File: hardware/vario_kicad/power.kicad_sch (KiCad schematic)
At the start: 26 parts, among them Q1 NMOS, Q2 PMOS, U4 USB C connector

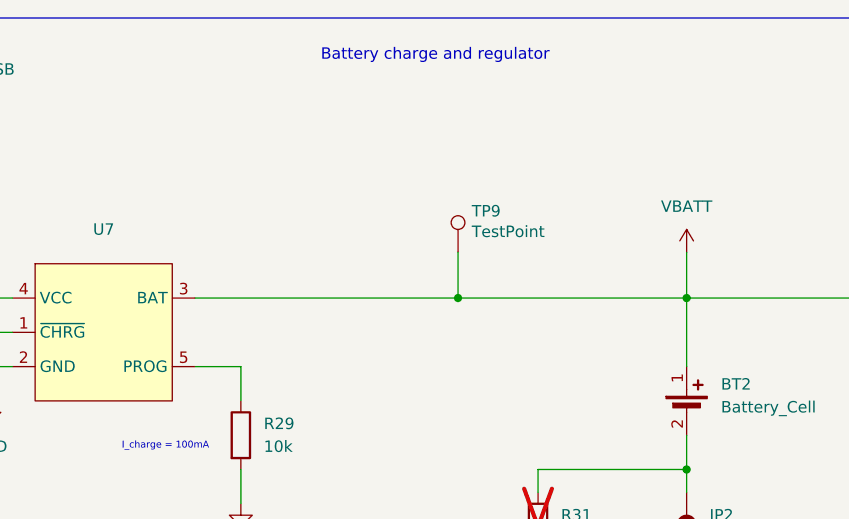
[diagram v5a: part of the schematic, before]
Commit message: add solder bridge to disconnect battery from charger
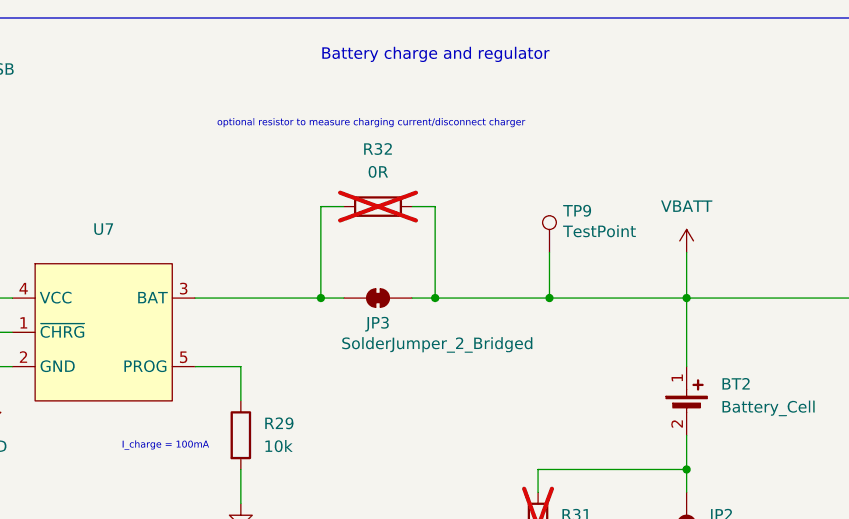
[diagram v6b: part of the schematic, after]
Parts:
- added JP3: SolderJumper_2_Bridged, Jumper:SolderJumper-2_P1.3mm_Open_TrianglePad1.0x1.5mm, symbol Jumper:SolderJumper_2_Bridged
- added R32: 0R, symbol Device:R
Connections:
- net VBATT: now also JP3.2 (B), R32.2; no longer U7.3 (BAT)
- new net: JP3.1 (A), R32.1, U7.3 (BAT)
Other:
- note added: "optional resistor to measure charging current/disconnect charger"
- moved on the sheet: TP9
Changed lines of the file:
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@@
 	)
 	(junction
+		(at 138.43 46.99)
+		(diameter 0)
+		(color 0 0 0 0)
+	)
+	(junction
 		(at 166.37 78.74)
 		(diameter 0)
@@
 	)
 	(junction
+		(at 125.73 46.99)
+		(diameter 0)
+		(color 0 0 0 0)
+	)
+	(junction
 		(at 41.91 149.86)
 		(diameter 0)
@@
 	)
 	(junction
+		(at 151.13 46.99)
+		(diameter 0)
+		(color 0 0 0 0)
+	)
+	(junction
 		(at 76.2 29.21)
 		(diameter 0)
@@
 	)
 	(junction
-		(at 140.97 46.99)
-		(diameter 0)
-		(color 0 0 0 0)
-	)
-	(junction
 		(at 214.63 59.69)
 		(diameter 0)
@@
 	(wire
 		(pts
+			(xy 128.27 46.99) (xy 125.73 46.99)
+		)
+		(stroke
+			(width 0)
+			(type default)
+		)
+	)
+	(wire
+		(pts
 			(xy 153.67 110.49) (xy 160.02 110.49)
 		)
@@
 	(wire
 		(pts
+			(xy 128.27 36.83) (xy 125.73 36.83)
+		)
+		(stroke
+			(width 0)
+			(type default)
+		)
+	)
+	(wire
+		(pts
 			(xy 30.48 149.86) (xy 41.91 149.86)
 		)
@@
 	(wire
 		(pts
+			(xy 125.73 36.83) (xy 125.73 46.99)
+		)
+		(stroke
+			(width 0)
+			(type default)
+		)
+	)
+	(wire
+		(pts
 			(xy 214.63 59.69) (xy 214.63 62.23)
 		)
@@
 	(wire
 		(pts
-			(xy 140.97 41.91) (xy 140.97 46.99)
+			(xy 151.13 41.91) (xy 151.13 46.99)
 		)
 		(stroke
@@
 	(wire
 		(pts
-			(xy 140.97 46.99) (xy 166.37 46.99)
+			(xy 151.13 46.99) (xy 166.37 46.99)
 		)
 		(stroke
@@
 	(wire
 		(pts
-			(xy 111.76 46.99) (xy 140.97 46.99)
-		)
-		(stroke
-			(width 0)
-			(type default)
-		)
-	)
-	(wire
-		(pts
 			(xy 44.45 109.22) (xy 50.8 109.22)
 		)
@@
 	(wire
 		(pts
+			(xy 138.43 46.99) (xy 135.89 46.99)
+		)
+		(stroke
+			(width 0)
+			(type default)
+		)
+	)
+	(wire
+		(pts
 			(xy 30.48 118.11) (xy 43.18 118.11)
 		)
@@
 	(wire
 		(pts
+			(xy 138.43 46.99) (xy 151.13 46.99)
+		)
+		(stroke
+			(width 0)
+			(type default)
+		)
+	)
+	(wire
+		(pts
+			(xy 138.43 36.83) (xy 135.89 36.83)
+		)
+		(stroke
+			(width 0)
+			(type default)
+		)
+	)
+	(wire
+		(pts
 			(xy 142.24 133.35) (xy 160.02 133.35)
 		)
@@
 	(wire
 		(pts
+			(xy 111.76 46.99) (xy 125.73 46.99)
+		)
+		(stroke
+			(width 0)
+			(type default)
+		)
+	)
+	(wire
+		(pts
 			(xy 166.37 46.99) (xy 166.37 54.61)
 		)
@@
 	(wire
 		(pts
+			(xy 138.43 46.99) (xy 138.43 36.83)
+		)
+		(stroke
+			(width 0)
+			(type default)
+		)
+	)
+	(wire
+		(pts
 			(xy 166.37 76.2) (xy 166.37 78.74)
 		)
@@
 		)
 	)
+	(text "optional resistor to measure charging current/disconnect charger"
+		(exclude_from_sim no)
+		(at 131.318 27.686 0)
+		(effects
+			(font
+				(size 0.762 0.762)
+			)
+		)
+	)
 	(text "Max V_BATT voltage 4.3V\nmax adc voltage 2.95V"
 		(exclude_from_sim no)
@@
 	)
 	(symbol
+		(lib_id "Jumper:SolderJumper_2_Bridged")
+		(at 132.08 46.99 0)
+		(unit 1)
+		(exclude_from_sim yes)
+		(in_bom no)
+		(on_board yes)
+		(dnp no)
+		(property "Reference" "JP3"
+			(at 132.08 49.784 0)
+			(effects
+				(font
+					(size 1.27 1.27)
+				)
+			)
+		)
+		(property "Value" "SolderJumper_2_Bridged"
+			(at 138.684 52.07 0)
+			(effects
+				(font
+					(size 1.27 1.27)
+				)
+			)
+		)
+		(property "Footprint" "Jumper:SolderJumper-2_P1.3mm_Open_TrianglePad1.0x1.5mm"
+			(at 132.08 46.99 0)
+			(effects
+				(font
+					(size 1.27 1.27)
+				)
+				(hide yes)
+			)
+		)
+		(property "Datasheet" "~"
+			(at 132.08 46.99 0)
+			(effects
+				(font
+					(size 1.27 1.27)
+				)
+				(hide yes)
+			)
+		)
+		(property "Description" "Solder Jumper, 2-pole, closed/bridged"
+			(at 132.08 46.99 0)
+			(effects
+				(font
+					(size 1.27 1.27)
+				)
+				(hide yes)
+			)
+		)
+		(pin "1"
+		)
+		(pin "2"
+		)
+		(instances
+			(project "vario_kicad"
+				(path "/50389aff-b244-451e-8e3a-c5addd2215e1/9ff7b2dd-70fe-4259-884c-1f1f10c7ad3d"
+					(reference "JP3")
+					(unit 1)
+				)
+			)
+		)
+	)
+	(symbol
 		(lib_id "Device:C")
 		(at 237.49 53.34 0)
@@
 	)
 	(symbol
+		(lib_id "Device:R")
+		(at 132.08 36.83 90)
+		(unit 1)
+		(exclude_from_sim no)
+		(in_bom yes)
+		(on_board yes)
+		(dnp yes)
+		(fields_autoplaced yes)
+		(property "Reference" "R32"
+			(at 132.08 30.48 90)
+			(effects
+				(font
+					(size 1.27 1.27)
+				)
+			)
+		)
+		(property "Value" "0R"
+			(at 132.08 33.02 90)
+			(effects
+				(font
+					(size 1.27 1.27)
+				)
+			)
+		)
+		(property "Footprint" ""
+			(at 132.08 38.608 90)
+			(effects
+				(font
+					(size 1.27 1.27)
+				)
+				(hide yes)
+			)
+		)
+		(property "Datasheet" "~"
+			(at 132.08 36.83 0)
+			(effects
+				(font
+					(size 1.27 1.27)
+				)
+				(hide yes)
+			)
+		)
+		(property "Description" "Resistor"
+			(at 132.08 36.83 0)
+			(effects
+				(font
+					(size 1.27 1.27)
+				)
+				(hide yes)
+			)
+		)
+		(pin "2"
+		)
+		(pin "1"
+		)
+		(instances
+			(project "vario_kicad"
+				(path "/50389aff-b244-451e-8e3a-c5addd2215e1/9ff7b2dd-70fe-4259-884c-1f1f10c7ad3d"
+					(reference "R32")
+					(unit 1)
+				)
+			)
+		)
+	)
+	(symbol
 		(lib_id "power:GND")
 		(at 63.5 40.64 0)
@@
 	(symbol
 		(lib_id "Connector:TestPoint")
-		(at 140.97 41.91 0)
+		(at 151.13 41.91 0)
 		(unit 1)
 		(exclude_from_sim no)
@@
 		(dnp no)
 		(property "Reference" "TP9"
-			(at 142.494 37.338 0)
+			(at 152.654 37.338 0)
 			(effects
 				(font
@@
 		)
 		(property "Value" "TestPoint"
-			(at 142.494 39.624 0)
+			(at 152.654 39.624 0)
 			(effects
 				(font
@@
 		)
 		(property "Footprint" "TestPoint:TestPoint_Pad_D1.0mm"
-			(at 146.05 41.91 0)
+			(at 156.21 41.91 0)
 			(effects
 				(font
@@
 		)
 		(property "Datasheet" "~"
-			(at 146.05 41.91 0)
+			(at 156.21 41.91 0)
 			(effects
 				(font
@@
 		)
 		(property "Description" "test point"
-			(at 140.97 41.91 0)
+			(at 151.13 41.91 0)
 			(effects
 				(font
@@
 		)
 		(property "Sim.Pins" ""
-			(at 140.97 41.91 0)
+			(at 151.13 41.91 0)
 			(effects
 				(font

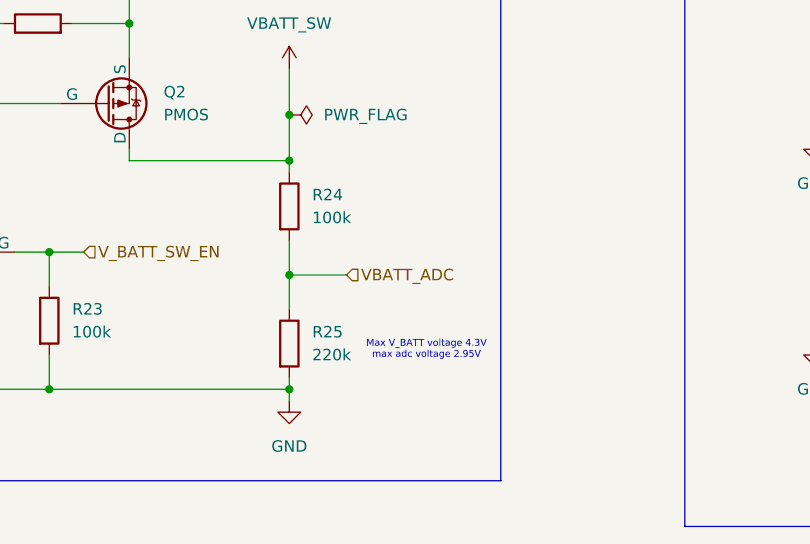
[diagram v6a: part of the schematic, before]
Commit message: smaller max value for BP voltage divider
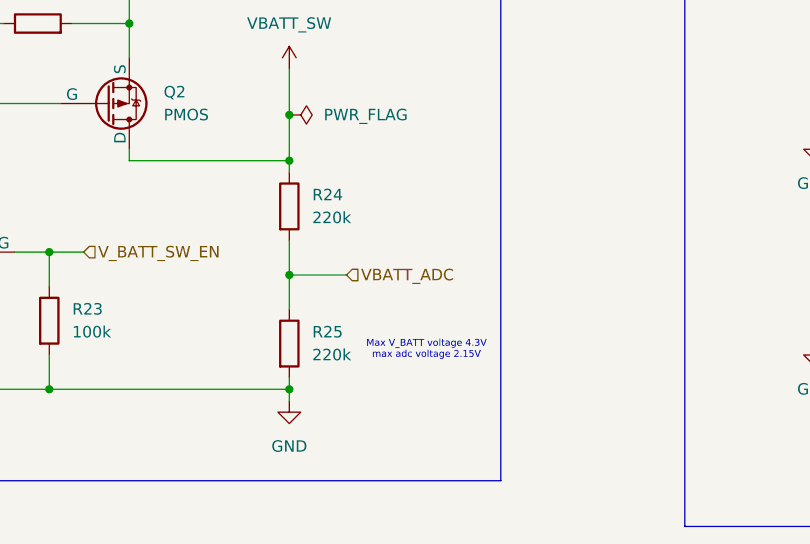
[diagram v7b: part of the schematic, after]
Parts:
- R24: value 100k -> 220k
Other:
- note added: "Max V_BATT voltage 4.3V max adc voltage 2.15V"
- note removed: "Max V_BATT voltage 4.3V max adc voltage 2.95V"
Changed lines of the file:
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@@
 		)
 	)
-	(text "Max V_BATT voltage 4.3V\nmax adc voltage 2.95V"
+	(text "Max V_BATT voltage 4.3V\nmax adc voltage 2.15V"
 		(exclude_from_sim no)
 		(at 83.82 145.542 0)
@@
 			)
 		)
-		(property "Value" "100k"
+		(property "Value" "220k"
 			(at 71.12 130.8099 0)
 			(effects

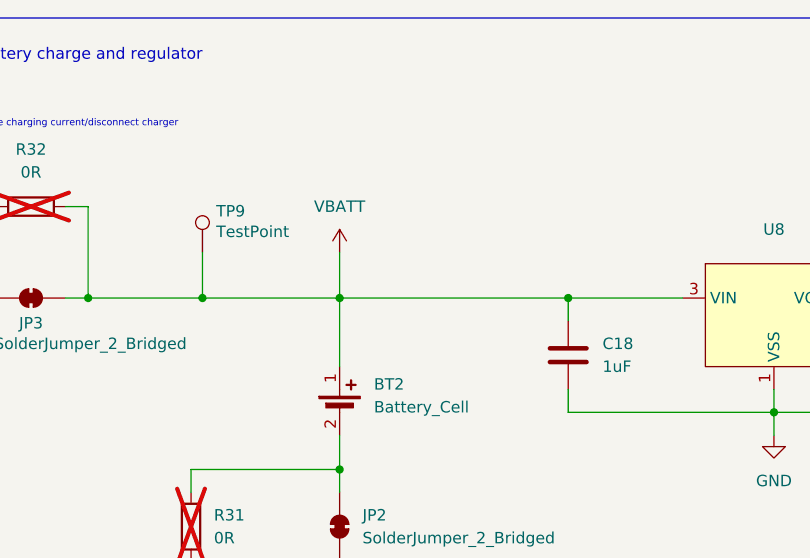
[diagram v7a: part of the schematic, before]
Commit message: add power symbol for ERC
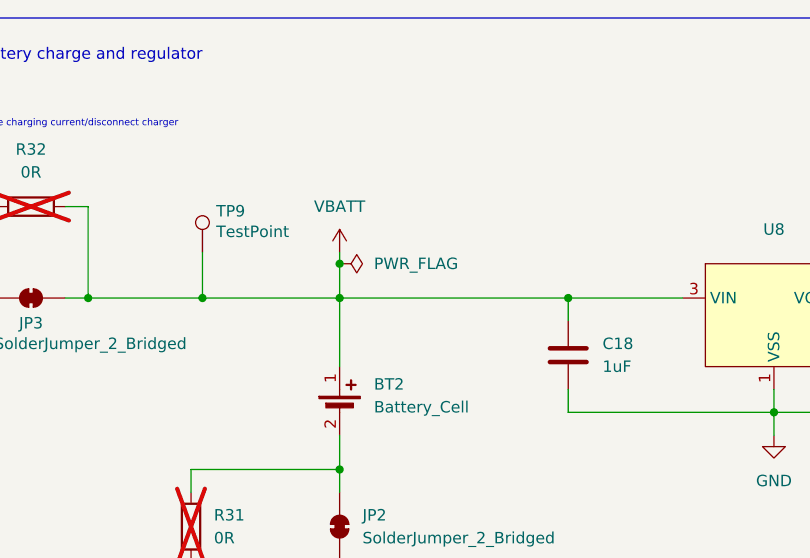
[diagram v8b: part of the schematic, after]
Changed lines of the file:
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@@
+	)
+	(junction
+		(at 166.37 43.18)
+		(diameter 0)
+		(color 0 0 0 0)
 	)
 	(junction
@@
 	(wire
 		(pts
-			(xy 166.37 41.91) (xy 166.37 46.99)
+			(xy 166.37 41.91) (xy 166.37 43.18)
 		)
 		(stroke
@@
 		(pts
 			(xy 88.9 46.99) (xy 91.44 46.99)
+		)
+		(stroke
+			(width 0)
+			(type default)
+		)
+	)
+	(wire
+		(pts
+			(xy 166.37 43.18) (xy 166.37 46.99)
 		)
 		(stroke
@@
 					(unit 1)
 				)
+			)
+		)
+	)
+	(symbol
+		(lib_id "power:PWR_FLAG")
+		(at 166.37 43.18 270)
+		(unit 1)
+		(exclude_from_sim no)
+		(in_bom yes)
+		(on_board yes)
+		(dnp no)
+		(fields_autoplaced yes)
+		(property "Reference" "#FLG1"
+			(at 168.275 43.18 0)
+			(effects
+				(font
+					(size 1.27 1.27)
+				)
+				(hide yes)
+			)
+		)
+		(property "Value" "PWR_FLAG"
+			(at 170.18 43.1799 90)
+			(effects
+				(font
+					(size 1.27 1.27)
+				)
+				(justify left)
+			)
+		)
+		(property "Footprint" ""
+			(at 166.37 43.18 0)
+			(effects
+				(font
+					(size 1.27 1.27)
+				)
+				(hide yes)
+			)
+		)
+		(property "Datasheet" "~"
+			(at 166.37 43.18 0)
+			(effects
+				(font
+					(size 1.27 1.27)
+				)
+				(hide yes)
+			)
+		)
+		(property "Description" "Special symbol for telling ERC where power comes from"
+			(at 166.37 43.18 0)
+			(effects
+				(font
+					(size 1.27 1.27)
+				)
+				(hide yes)
+			)
+		)
+		(pin "1"
+		)
+		(instances
+			(project ""
+				(path "/50389aff-b244-451e-8e3a-c5addd2215e1/9ff7b2dd-70fe-4259-884c-1f1f10c7ad3d"
+					(reference "#FLG1")
+					(unit 1)
+				)
